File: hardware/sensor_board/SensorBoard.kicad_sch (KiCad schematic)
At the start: 75 parts, among them J1 Relay Board Connector, J10 GND BUS, J11 FEED SENSOR R2, J13 SPARE GPIO, J15 LED L1, J16 LED L2, J17 LED L3, J18 LED L4, J19 LED R1, J2 Pi 5V, J20 EXT, J21 LED R2, J22 LED R3, J23 LED R4, J24 Raspberry Pi GPIO header, J25 RTC Header, J26 I2C0, J27 I2C1, J28 I2C2, J29 I2C3, J3 Display 5V, J30 I2C4, J31 I2C5, J32 I2C6, J33 I2C7, J4 DC IN 5V, J5 VSYS BUS, J6 FEED SENSOR L1, J7 3V3 BUS, J8 FEED SENSOR R1, J9 FEED SENSOR L2, Q1 PN2222A, Q2 PN2222A, Q3 PN2222A, Q4 PN2222A, Q5 PN2222A, Q6 PN2222A, Q7 PN2222A, Q8 PN2222A, SW1 Pico Reset, U1 Raspberry Pico, U2 74HC595, U3 TCA9548A, U4 LM1117, U5 DS3231MZ, U6 74HC165

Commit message: Final 3.0 tweakage. Gerbers sent to OSHPark
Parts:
- J11: value FEED SENSOR R2 -> FEED SENSOR R1
- J6: value FEED SENSOR L1 -> FEED SENSOR L2
- J8: value FEED SENSOR R1 -> FEED SENSOR R2
- J9: value FEED SENSOR L2 -> FEED SENSOR L1
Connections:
- net FEED SENSOR L1 DETECT: now also J9.4 (Pin_4), U1.5 (GPIO3); no longer J6.4 (Pin_4), U1.4 (GPIO2)
- net FEED SENSOR L1 RX: now also J9.5 (Pin_5), U1.10 (GPIO7); no longer J6.5 (Pin_5), U1.7 (GPIO5)
- net FEED SENSOR L1 TX: now also J9.2 (Pin_2), U1.9 (GPIO6); no longer J6.2 (Pin_2), U1.6 (GPIO4)
- net FEED SENSOR L2 DETECT: now also J6.4 (Pin_4), U1.4 (GPIO2); no longer J9.4 (Pin_4), U1.5 (GPIO3)
- net FEED SENSOR L2 RX: now also J6.5 (Pin_5), U1.7 (GPIO5); no longer J9.5 (Pin_5), U1.10 (GPIO7)
- net FEED SENSOR L2 TX: now also J6.2 (Pin_2), U1.6 (GPIO4); no longer J9.2 (Pin_2), U1.9 (GPIO6)
- net FEED SENSOR R1 DETECT: now also J11.4 (Pin_4), U1.1 (GPIO0); no longer J8.4 (Pin_4), U1.2 (GPIO1)
- net FEED SENSOR R1 RX: now also J11.5 (Pin_5), U1.29 (GPIO22); no longer J8.5 (Pin_5), U1.32 (GPIO27_ADC1)
- net FEED SENSOR R1 TX: now also J11.2 (Pin_2), U1.31 (GPIO26_ADC0); no longer J8.2 (Pin_2), U1.34 (GPIO28_ADC2)
- net FEED SENSOR R2 DETECT: now also J8.4 (Pin_4), U1.2 (GPIO1); no longer J11.4 (Pin_4), U1.1 (GPIO0)
- net FEED SENSOR R2 RX: now also J8.5 (Pin_5), U1.32 (GPIO27_ADC1); no longer J11.5 (Pin_5), U1.29 (GPIO22)
- net FEED SENSOR R2 TX: now also J8.2 (Pin_2), U1.34 (GPIO28_ADC2); no longer J11.2 (Pin_2), U1.31 (GPIO26_ADC0)
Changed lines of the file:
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@@
     (stroke (width 0) (type default) (color 0 0 0 0))
   )
-  (label "FEED SENSOR L1 TX" (at 138.43 177.8 0)
+  (label "FEED SENSOR L2 TX" (at 138.43 177.8 0)
     (effects (font (size 1.27 1.27)) (justify left bottom))
   )
@@
     (effects (font (size 1.27 1.27)) (justify left bottom))
   )
-  (label "FEED SENSOR R1 TX" (at 219.71 172.72 0)
-    (effects (font (size 1.27 1.27)) (justify left bottom))
-  )
-  (label "FEED SENSOR R2 RX" (at 219.71 195.58 0)
+  (label "FEED SENSOR R2 TX" (at 219.71 172.72 0)
+    (effects (font (size 1.27 1.27)) (justify left bottom))
+  )
+  (label "FEED SENSOR R1 RX" (at 219.71 195.58 0)
     (effects (font (size 1.27 1.27)) (justify left bottom))
   )
@@
     (effects (font (size 1.27 1.27)) (justify right bottom))
   )
-  (label "FEED SENSOR L2 TX" (at 128.27 185.42 0)
+  (label "FEED SENSOR L1 TX" (at 128.27 185.42 0)
     (effects (font (size 1.27 1.27)) (justify left bottom))
   )
@@
     (effects (font (size 1.27 1.27)) (justify left bottom))
   )
-  (label "FEED SENSOR L2 RX" (at 128.27 187.96 0)
-    (effects (font (size 1.27 1.27)) (justify left bottom))
-  )
-  (label "FEED SENSOR L1 DETECT" (at 138.43 172.72 0)
-    (effects (font (size 1.27 1.27)) (justify left bottom))
-  )
-  (label "FEED SENSOR R2 DETECT" (at 175.26 152.4 0)
+  (label "FEED SENSOR L1 RX" (at 128.27 187.96 0)
+    (effects (font (size 1.27 1.27)) (justify left bottom))
+  )
+  (label "FEED SENSOR L2 DETECT" (at 138.43 172.72 0)
+    (effects (font (size 1.27 1.27)) (justify left bottom))
+  )
+  (label "FEED SENSOR R1 DETECT" (at 175.26 152.4 0)
     (effects (font (size 1.27 1.27)) (justify left bottom))
   )
@@
     (effects (font (size 1.27 1.27)) (justify left bottom))
   )
-  (label "FEED SENSOR R1 DETECT" (at 175.26 154.94 0)
-    (effects (font (size 1.27 1.27)) (justify left bottom))
-  )
-  (label "FEED SENSOR R2 TX" (at 219.71 187.96 0)
+  (label "FEED SENSOR R2 DETECT" (at 175.26 154.94 0)
+    (effects (font (size 1.27 1.27)) (justify left bottom))
+  )
+  (label "FEED SENSOR R1 TX" (at 219.71 187.96 0)
     (effects (font (size 1.27 1.27)) (justify left bottom))
   )
@@
     (effects (font (size 1.27 1.27)) (justify right bottom))
   )
-  (label "FEED SENSOR L1 RX" (at 138.43 180.34 0)
-    (effects (font (size 1.27 1.27)) (justify left bottom))
-  )
-  (label "FEED SENSOR R1 RX" (at 219.71 180.34 0)
+  (label "FEED SENSOR L2 RX" (at 138.43 180.34 0)
+    (effects (font (size 1.27 1.27)) (justify left bottom))
+  )
+  (label "FEED SENSOR R2 RX" (at 219.71 180.34 0)
     (effects (font (size 1.27 1.27)) (justify left bottom))
   )
@@
     (effects (font (size 1.27 1.27)) (justify left bottom))
   )
-  (label "FEED SENSOR L2 DETECT" (at 138.43 175.26 0)
+  (label "FEED SENSOR L1 DETECT" (at 138.43 175.26 0)
     (effects (font (size 1.27 1.27)) (justify left bottom))
   )
@@
       (effects (font (size 1.27 1.27)) (justify left))
     )
-    (property "Value" "FEED SENSOR R2" (id 1) (at 248.92 191.7699 0)
+    (property "Value" "FEED SENSOR R1" (id 1) (at 248.92 191.7699 0)
       (effects (font (size 1.27 1.27)) (justify left))
     )
@@
       (effects (font (size 1.27 1.27)) (justify left))
     )
-    (property "Value" "FEED SENSOR R1" (id 1) (at 248.92 176.5299 0)
+    (property "Value" "FEED SENSOR R2" (id 1) (at 248.92 176.5299 0)
       (effects (font (size 1.27 1.27)) (justify left))
     )
@@
       (effects (font (size 1.27 1.27)) (justify right))
     )
-    (property "Value" "FEED SENSOR L2" (id 1) (at 99.06 165.1 90)
+    (property "Value" "FEED SENSOR L1" (id 1) (at 99.06 165.1 90)
       (effects (font (size 1.27 1.27)) (justify right))
     )
@@
     (in_bom yes) (on_board yes)
     (property "Reference" "J6" (id 0) (at 96.52 153.67 90))
-    (property "Value" "FEED SENSOR L1" (id 1) (at 99.06 146.05 90)
+    (property "Value" "FEED SENSOR L2" (id 1) (at 99.06 146.05 90)
       (effects (font (size 1.27 1.27)) (justify right))
     )
@@
     )
     (path "/d20d88ab-1692-4800-81c7-56eafc1d29af"
-      (reference "J6") (unit 1) (value "FEED SENSOR L1") (footprint "Connector_JST:JST_XH_B5B-XH-A_1x05_P2.50mm_Vertical")
+      (reference "J6") (unit 1) (value "FEED SENSOR L2") (footprint "Connector_JST:JST_XH_B5B-XH-A_1x05_P2.50mm_Vertical")
     )
     (path "/321ae696-bd7f-4a5c-9195-899bf2dfc30c"
@@
     )
     (path "/4300da7b-665e-42b0-a1bc-db201ad6d1a7"
-      (reference "J8") (unit 1) (value "FEED SENSOR R1") (footprint "Connector_JST:JST_XH_B5B-XH-A_1x05_P2.50mm_Vertical")
+      (reference "J8") (unit 1) (value "FEED SENSOR R2") (footprint "Connector_JST:JST_XH_B5B-XH-A_1x05_P2.50mm_Vertical")
     )
     (path "/4ef651eb-b121-4989-b5a2-5f980b8583ca"
-      (reference "J9") (unit 1) (value "FEED SENSOR L2") (footprint "Connector_JST:JST_XH_B5B-XH-A_1x05_P2.50mm_Vertical")
+      (reference "J9") (unit 1) (value "FEED SENSOR L1") (footprint "Connector_JST:JST_XH_B5B-XH-A_1x05_P2.50mm_Vertical")
     )
     (path "/e72c4d5e-d53f-4e40-b57d-5ecc90b511cd"
@@
     )
     (path "/366d3741-0207-4cd7-be77-4bec81ff3e78"
-      (reference "J11") (unit 1) (value "FEED SENSOR R2") (footprint "Connector_JST:JST_XH_B5B-XH-A_1x05_P2.50mm_Vertical")
+      (reference "J11") (unit 1) (value "FEED SENSOR R1") (footprint "Connector_JST:JST_XH_B5B-XH-A_1x05_P2.50mm_Vertical")
     )
     (path "/33c873bc-5175-4bde-be91-b4576bd776e4"

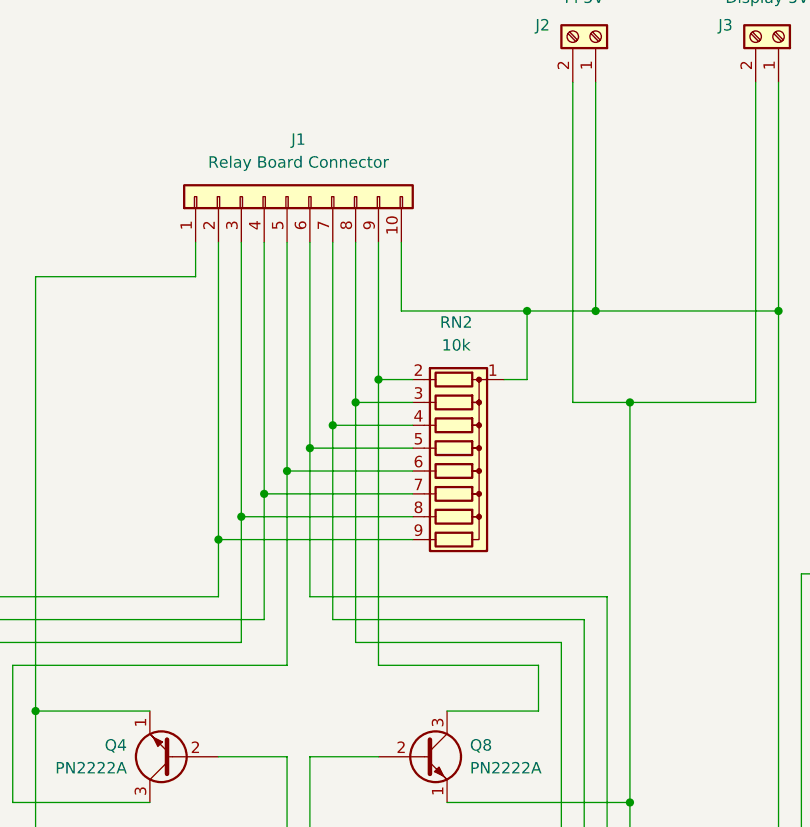
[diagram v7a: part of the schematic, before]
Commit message: Modifying HIB to include relay pull jumper (for defaulting relay inputs to HIGH or LOW on startup)
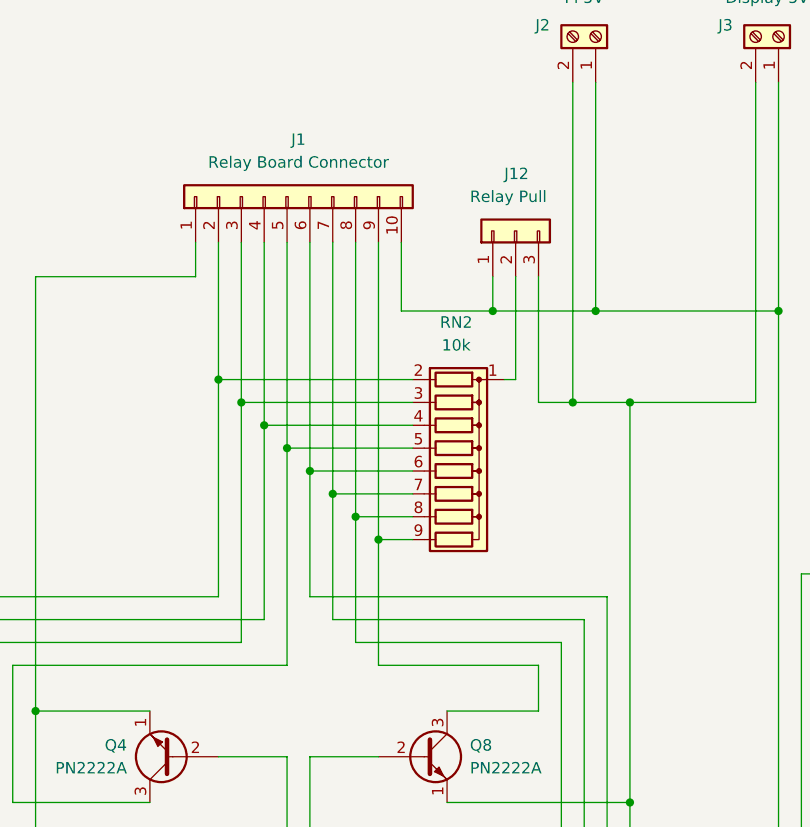
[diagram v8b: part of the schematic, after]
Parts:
- added J12: Relay Pull, Connector_PinHeader_2.54mm:PinHeader_1x03_P2.54mm_Vertical, symbol Connector_Generic:Conn_01x03
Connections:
- net GND: now also J12.3 (Pin_3)
- net VS: now also J12.1 (Pin_1); no longer RN2.1 (common)
- net at J1.7 (Pin_7), Q6.3 (C): now also RN2.7 (R6); no longer RN2.4 (R3)
- net at J1.2 (Pin_2), Q1.3 (C): now also RN2.2 (R1); no longer RN2.9 (R8)
- net at J1.9 (Pin_9), Q8.3 (C): now also RN2.9 (R8); no longer RN2.2 (R1)
- net at J1.8 (Pin_8), Q7.3 (C): now also RN2.8 (R7); no longer RN2.3 (R2)
- net at J1.6 (Pin_6), Q5.3 (C): now also RN2.6 (R5); no longer RN2.5 (R4)
- net at J1.5 (Pin_5), Q4.3 (C): now also RN2.5 (R4); no longer RN2.6 (R5)
- net at J1.4 (Pin_4), Q3.3 (C): now also RN2.4 (R3); no longer RN2.7 (R6)
- net at J1.3 (Pin_3), Q2.3 (C): now also RN2.3 (R2); no longer RN2.8 (R7)
- new net: J12.2 (Pin_2), RN2.1 (common)
